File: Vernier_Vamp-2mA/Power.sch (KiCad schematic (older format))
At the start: 69 parts, among them J4 Conn_02x07_Odd_Even, Q1 Si4447ADY, Q2 IRF8707PbF, SW1 DPDT_Hirose, U1 LM4040DBZ-5, U2 LM4040DBZ-5, U3 LM393, U4 TPS7A470x, U5 TPS7A470x, U6 TPS7A33

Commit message: 1.0B fixes for 2mA (schematic)
Added 1.0B fixes to the 2mA version related to schematic cleanup, and addition of hysteresis and alternative way to power nano.
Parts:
- removed C56, C57, C58, C59, C62, C63: 100n, Capacitor_SMD:C_0603_1608Metric_Pad1.05x0.95mm_HandSolder, symbol Device:C_Small
- removed D3, D4, D5, D6: SMBJ16A, Diode_SMD:D_SMB_Handsoldering, symbol SMBJ15A:SMBJ15A
- removed F1, F2: 1A, Fuse:Fuse_1812_4532Metric_Pad1.30x3.40mm_HandSolder, symbol Device:Polyfuse_Small
- removed H1, H2, H3, H4, H5: MountingHole_Pad, MountingHole:MountingHole_3.2mm_M3_Pad_Via, symbol Mechanical:MountingHole_Pad
- removed J4: Conn_02x07_Odd_Even, Connector_Hirose:Hirose_DF11-14DP-2DSA_2x07_P2.00mm_Vertical, symbol Connector_Generic:Conn_02x07_Odd_Even
- removed Q1: Si4447ADY, Package_SO:SO-8_3.9x4.9mm_P1.27mm, symbol Si4447ADY:Si4447ADY
- removed Q2: IRF8707PbF, Package_SO:SO-8_3.9x4.9mm_P1.27mm, symbol IRF8707PbF:IRF8707PbF
- removed R1, R11, R12, R15, R16, R17, R2, R3, R4, R5, R6: 10k, Resistor_SMD:R_0603_1608Metric_Pad1.05x0.95mm_HandSolder, symbol Device:R_Small
- removed R10, R8: 100k, Resistor_SMD:R_0603_1608Metric_Pad1.05x0.95mm_HandSolder, symbol Device:R_Small
- removed R7, R9: 120k, Resistor_SMD:R_0603_1608Metric_Pad1.05x0.95mm_HandSolder, symbol Device:R_Small
- removed SW1: DPDT_Hirose, Connector_Hirose:Hirose_DF11-6DP-2DSA_2x03_P2.00mm_Vertical, symbol SW_DPDT_Hirose:DPDT_Hirose
- removed TP1, TP10, TP11, TP2, TP3, TP4, TP5, TP6, TP7, TP8, TP9: TestPoint_Probe, TestPoint:TestPoint_Pad_D1.0mm, symbol Connector:TestPoint_Probe
- removed U1, U2: LM4040DBZ-5, Package_TO_SOT_SMD:SOT-23, symbol Reference_Voltage:LM4040DBZ-5
- removed U3: LM393, Package_SO:TSSOP-8_4.4x3mm_P0.65mm, symbol Comparator:LM393
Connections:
- net labels added: +7.5V, -7.5V
- net labels removed: +5VD, +5V_c_ref, +8V, +BATT, -5V_c_ref, -8V, -BATT, LED1_N, LED1_P, LED2_N, LED2_P, LED3_N, LED3_P, LED4_N, LED4_P, LED5_N, LED5_P, LED6_N, LED6_P, LED7_N, LED7_P
- wire segments 254 -> 100
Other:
- note added: "Ultra low noise LDO, configured to provide +7.5VDC"
- note removed: "Extra redundancy passive protection\nLimits the supply to 16.7V\nUses PPTC as a resetable fuse"
- note removed: "Low battery indicator (< 11V)\n"
- note removed: "Panel LED\nconnector"
- note removed: "Positive/Negative active protection\ncircuit\nTVS used to limit GS voltage\nalso used for ESD protection"
- note removed: "Reverse polarity protection\n"
- note removed: "Soft On/Off DPDT switch\n"
- note removed: "Ultra low noise LDO, configured to provide +7.5VDC (ignore +8V label)"
- moved on the sheet: C10, C11, C12, C13, C4, C5, C6, C7, C8, C9, R13, R14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

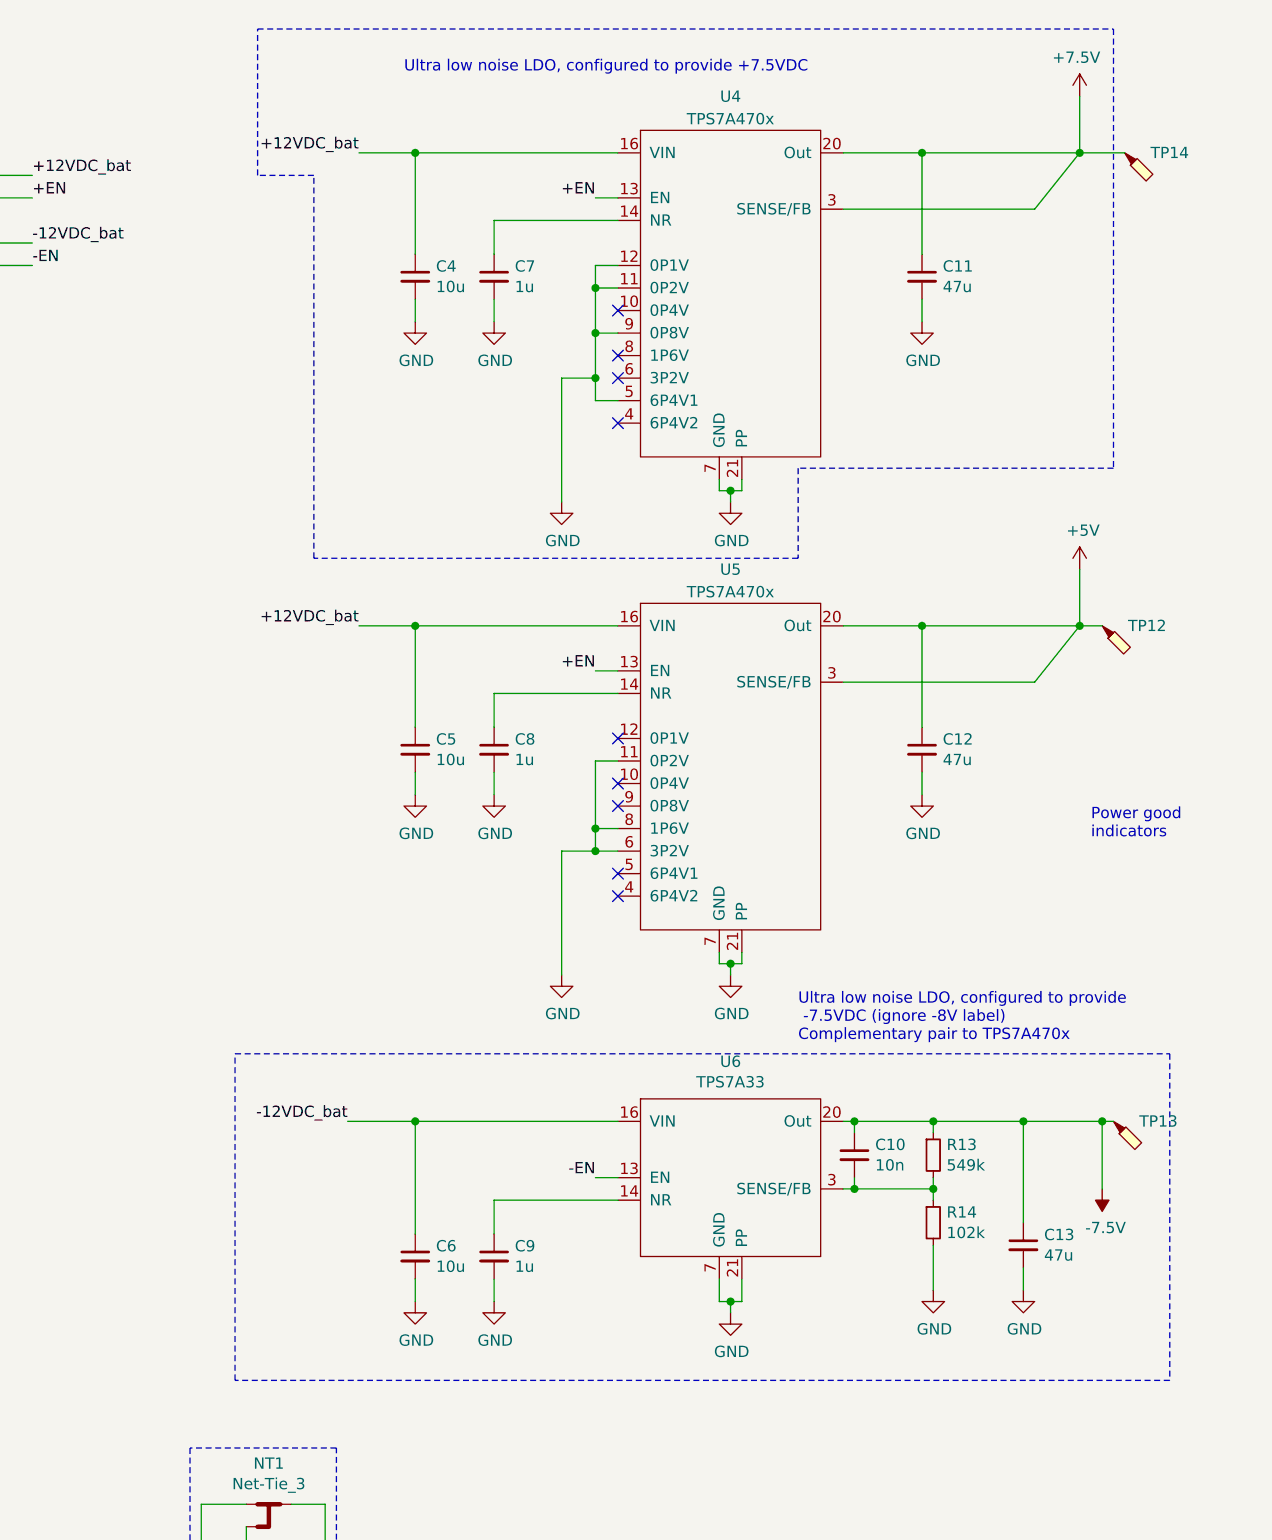
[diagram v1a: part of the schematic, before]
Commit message: Applied 1.0B changes to 2mA version
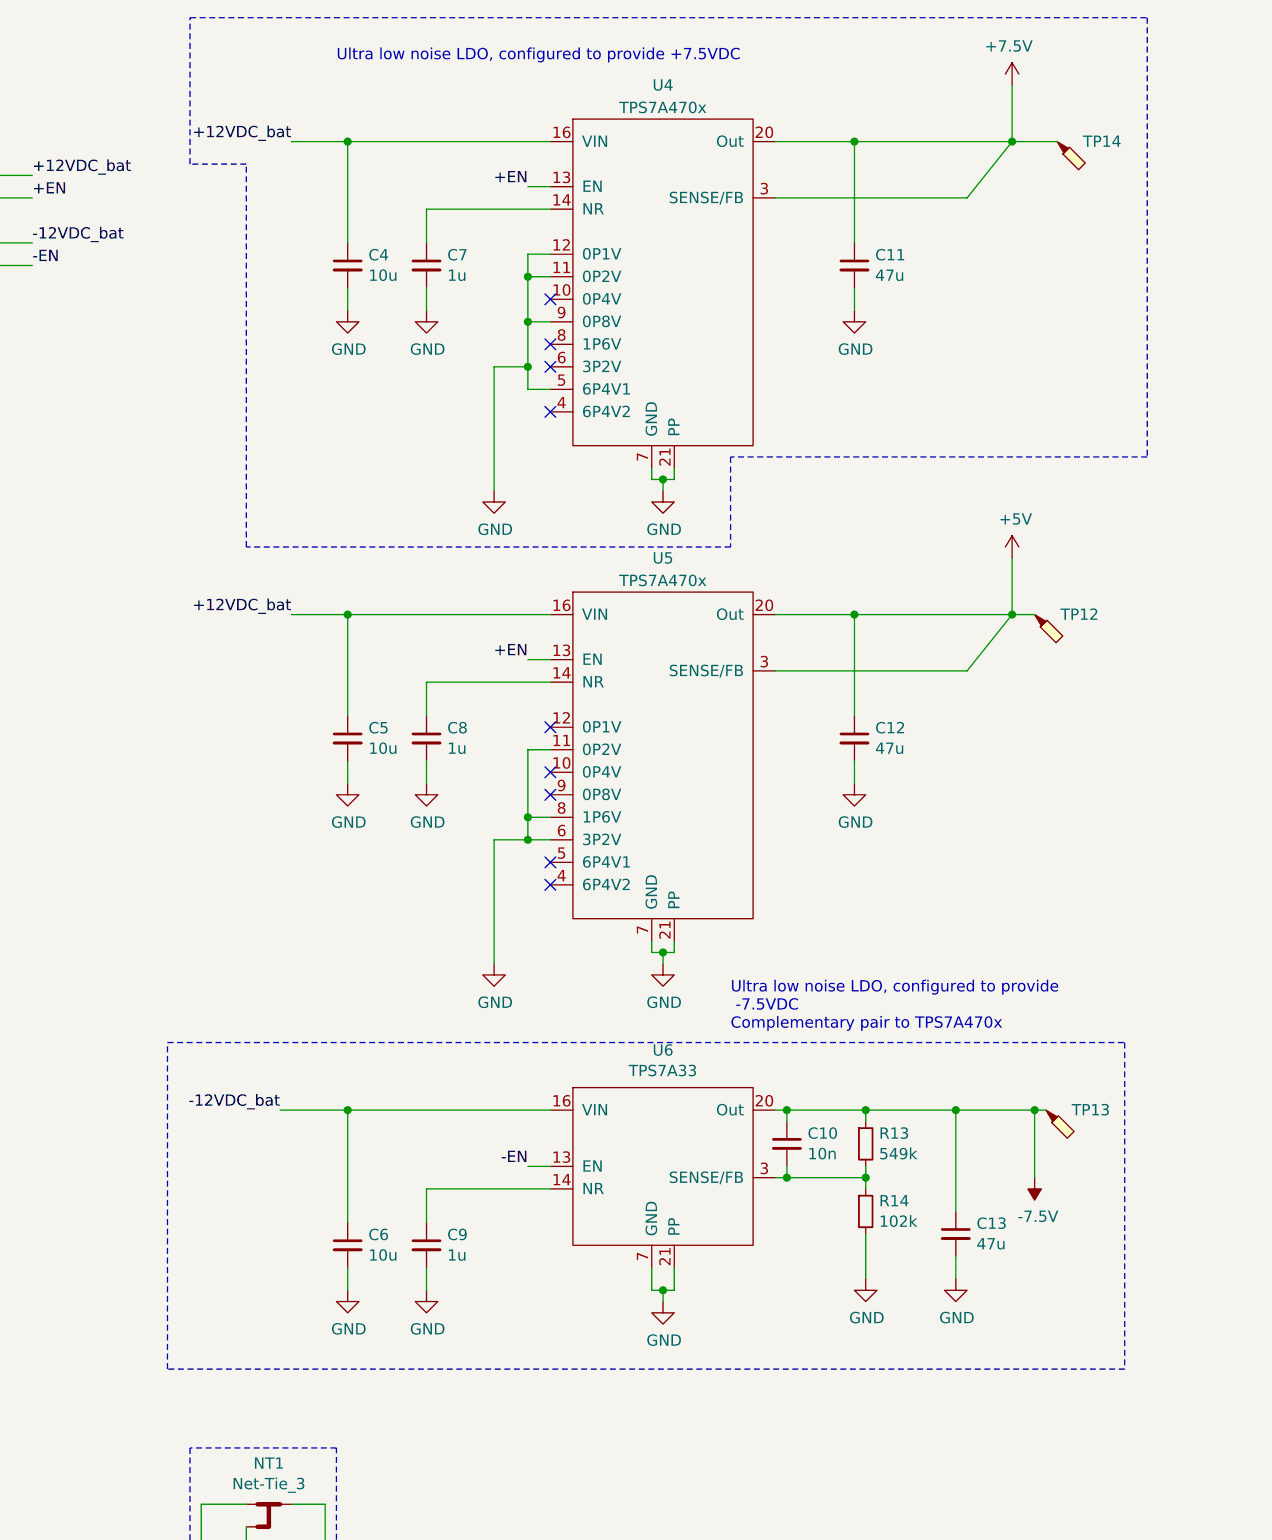
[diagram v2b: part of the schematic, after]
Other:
- note added: "Ultra low noise LDO, configured to provide\n -7.5VDC \nComplementary pair to TPS7A470x"
- note removed: "Power good\nindicators"
- note removed: "Ultra low noise LDO, configured to provide\n -7.5VDC (ignore -8V label)\nComplementary pair to TPS7A470x"
- moved on the sheet: C10, C11, C12, C13, C4, C5, C6, C7, C8, C9, R13, R14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

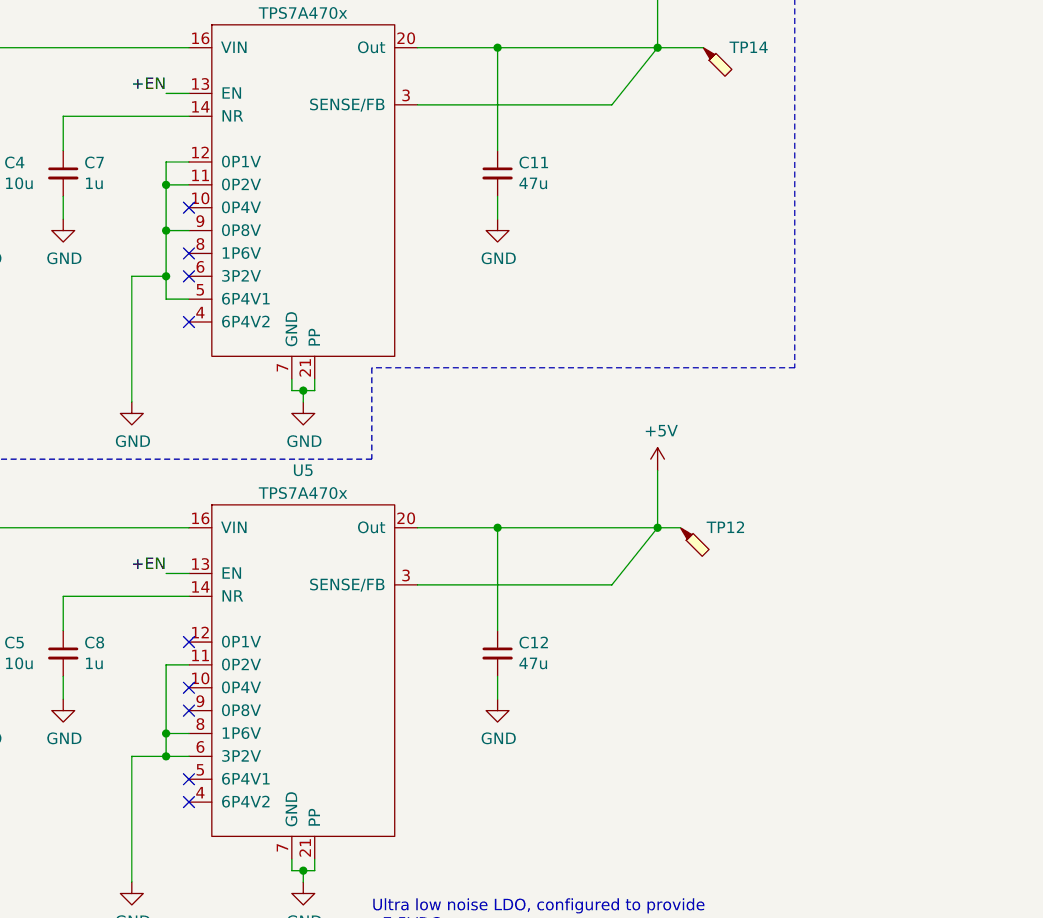
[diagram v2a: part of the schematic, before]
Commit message: Fixed LDO programmable output
Fixed the LDO so that the output matches with programmed one.
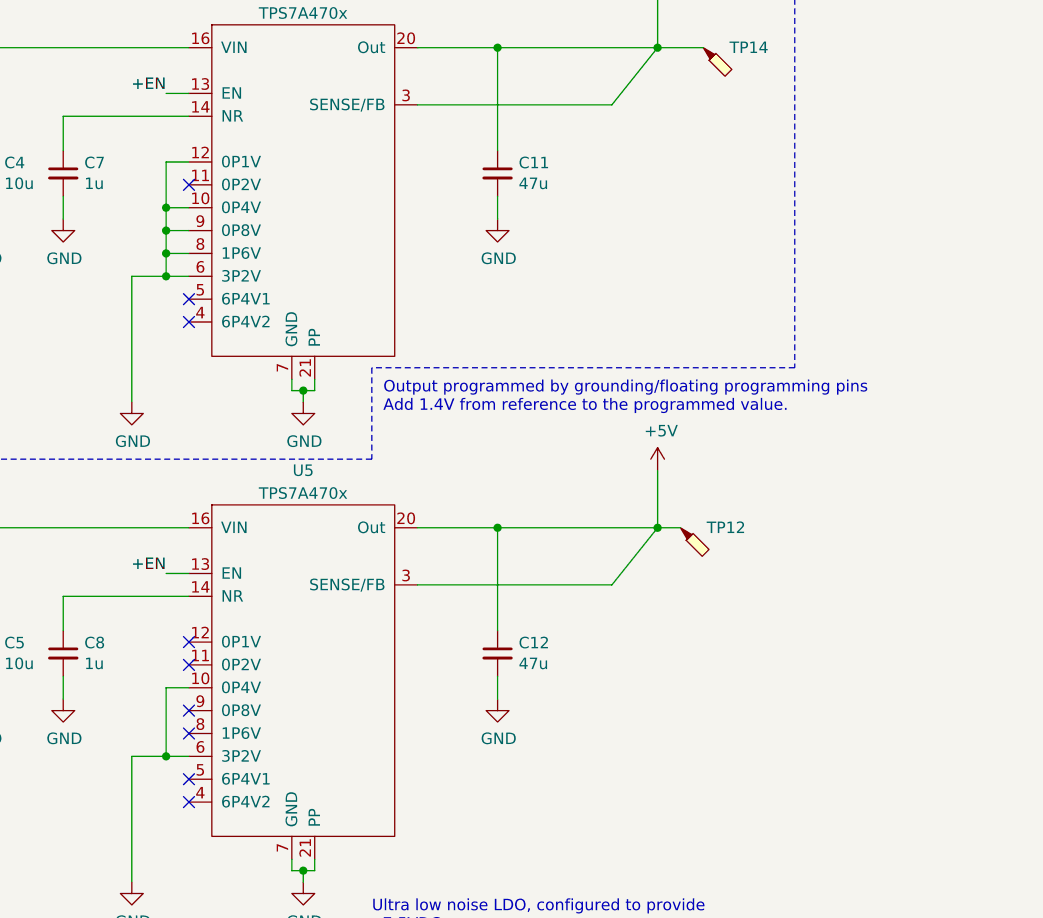
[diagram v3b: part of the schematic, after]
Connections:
- net GND: now also U4.10 (0P4V), U4.6 (3P2V), U4.8 (1P6V), U5.10 (0P4V); no longer U4.11 (0P2V), U4.5 (6P4V1), U5.11 (0P2V), U5.8 (1P6V)
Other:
- note added: "Output programmed by grounding/floating programming pins\nAdd 1.4V from reference to the programmed value."
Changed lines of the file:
@@
 Comment4 ""
 $EndDescr
-Wire Wire Line
-	5250 2150 5150 2150
-Wire Wire Line
-	5150 2050 5150 2150
 $Comp
 L power:GND #PWR0101
@@
 Wire Wire Line
 	4700 1700 4700 1800
-Connection ~ 5150 2050
 Wire Wire Line
 	5150 2050 5000 2050
@@
 	5000 2050 5000 2600
 NoConn ~ 5250 2250
-NoConn ~ 5250 1950
 $Comp
 L Device:C_Small C4
@@
 	6250 3400 7100 3400
 Connection ~ 6600 3150
-NoConn ~ 5250 3850
-Wire Wire Line
-	5250 4050 5150 4050
-Wire Wire Line
-	5150 4050 5150 4150
-Wire Wire Line
-	5250 3750 5150 3750
-Wire Wire Line
-	5150 3750 5150 4050
-Connection ~ 5150 4050
 NoConn ~ 5250 4250
 Text Label 5150 1250 2    50   ~ 0
@@
 Wire Wire Line
 	4350 3150 5250 3150
-NoConn ~ 5250 2050
-NoConn ~ 5250 1750
 Wire Wire Line
 	5250 1550 5150 1550
-Wire Wire Line
-	5150 1550 5150 1650
-Wire Wire Line
-	5250 1650 5150 1650
-Connection ~ 5150 1650
-Wire Wire Line
-	5150 1650 5150 1850
 Wire Wire Line
 	5250 1850 5150 1850
 Connection ~ 5150 1850
 Wire Wire Line
-	5150 1850 5150 2050
+	5150 1850 5150 1950
 Text Notes 3650 7650 0    50   ~ 0
 Star ground point\n
@@
 F8 "-EN" O R 2800 1600 50
 $EndSheet
+Text Notes 6100 2650 0    50   ~ 0
+Output programmed by grounding/floating programming pins\nAdd 1.4V from reference to the programmed value.
+Wire Wire Line
+	5150 1550 5150 1750
+Wire Wire Line
+	5250 1750 5150 1750
+Connection ~ 5150 1750
+Wire Wire Line
+	5150 1750 5150 1850
+Wire Wire Line
+	5250 1950 5150 1950
+Connection ~ 5150 1950
+Wire Wire Line
+	5150 1950 5150 2050
+Wire Wire Line
+	5250 2050 5150 2050
+Connection ~ 5150 2050
+NoConn ~ 5250 1650
+NoConn ~ 5250 2150
+NoConn ~ 5250 3750
+NoConn ~ 5250 4050
+Wire Wire Line
+	5250 3850 5150 3850
+Wire Wire Line
+	5150 3850 5150 4150
 $EndSCHEMATC

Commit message: 1.0C Initial commit
-Fixed amplifier output
-Changed connectors to IDC
-Via perimeter added
TODO:
Add shielding over analogue section
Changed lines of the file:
@@
 Wire Wire Line
 	4700 1700 4700 1800
-Wire Wire Line
-	5150 2050 5000 2050
-Wire Wire Line
-	5000 2050 5000 2600
 NoConn ~ 5250 2250
 $Comp
@@
 	6250 1300 7100 1300
 Connection ~ 6600 1050
-Wire Wire Line
-	5250 4150 5150 4150
 $Comp
 L power:GND #PWR0122
@@
 Wire Wire Line
 	4700 3800 4700 3900
-Connection ~ 5150 4150
-Wire Wire Line
-	5150 4150 5000 4150
 Wire Wire Line
 	5000 4150 5000 4700
 NoConn ~ 5250 4350
-NoConn ~ 5250 3650
-NoConn ~ 5250 3950
 $Comp
 L Device:C_Small C5
@@
 Wire Wire Line
 	4350 3150 5250 3150
-Wire Wire Line
-	5250 1550 5150 1550
-Wire Wire Line
-	5250 1850 5150 1850
-Connection ~ 5150 1850
-Wire Wire Line
-	5150 1850 5150 1950
 Text Notes 3650 7650 0    50   ~ 0
 Star ground point\n
@@
 Text Notes 6100 2650 0    50   ~ 0
 Output programmed by grounding/floating programming pins\nAdd 1.4V from reference to the programmed value.
-Wire Wire Line
-	5150 1550 5150 1750
-Wire Wire Line
-	5250 1750 5150 1750
-Connection ~ 5150 1750
-Wire Wire Line
-	5150 1750 5150 1850
-Wire Wire Line
-	5250 1950 5150 1950
-Connection ~ 5150 1950
-Wire Wire Line
-	5150 1950 5150 2050
-Wire Wire Line
-	5250 2050 5150 2050
-Connection ~ 5150 2050
 NoConn ~ 5250 1650
 NoConn ~ 5250 2150
@@
 NoConn ~ 5250 4050
 Wire Wire Line
-	5250 3850 5150 3850
-Wire Wire Line
-	5150 3850 5150 4150
+	5000 4150 5250 4150
+Wire Wire Line
+	5000 3850 5000 4150
+Connection ~ 5000 4150
+NoConn ~ 5250 3650
+NoConn ~ 5250 3950
+Wire Wire Line
+	5000 1550 5250 1550
+Wire Wire Line
+	5000 3850 5250 3850
+Wire Wire Line
+	5000 1550 5000 1750
+Connection ~ 5000 1750
+Wire Wire Line
+	5000 1750 5000 1850
+Wire Wire Line
+	5000 1750 5250 1750
+Connection ~ 5000 1850
+Wire Wire Line
+	5000 1850 5000 1950
+Wire Wire Line
+	5000 1850 5250 1850
+Connection ~ 5000 1950
+Wire Wire Line
+	5000 1950 5000 2050
+Wire Wire Line
+	5000 1950 5250 1950
+Wire Wire Line
+	5000 2050 5250 2050
+Connection ~ 5000 2050
+Wire Wire Line
+	5000 2050 5000 2600
 $EndSCHEMATC
